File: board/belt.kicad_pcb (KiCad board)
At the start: 2 copper layers, 21 parts, among them J1 USB_B_Micro, J2 USB_B_Micro, J3 USB_B_Micro, J4 USB_B_Micro, Q1 BSS138, Q2 BSS138, SW1 SW_SPST, SW2 SW_Push, U1 Teensy4.0, U2 Adafruit_BNO055

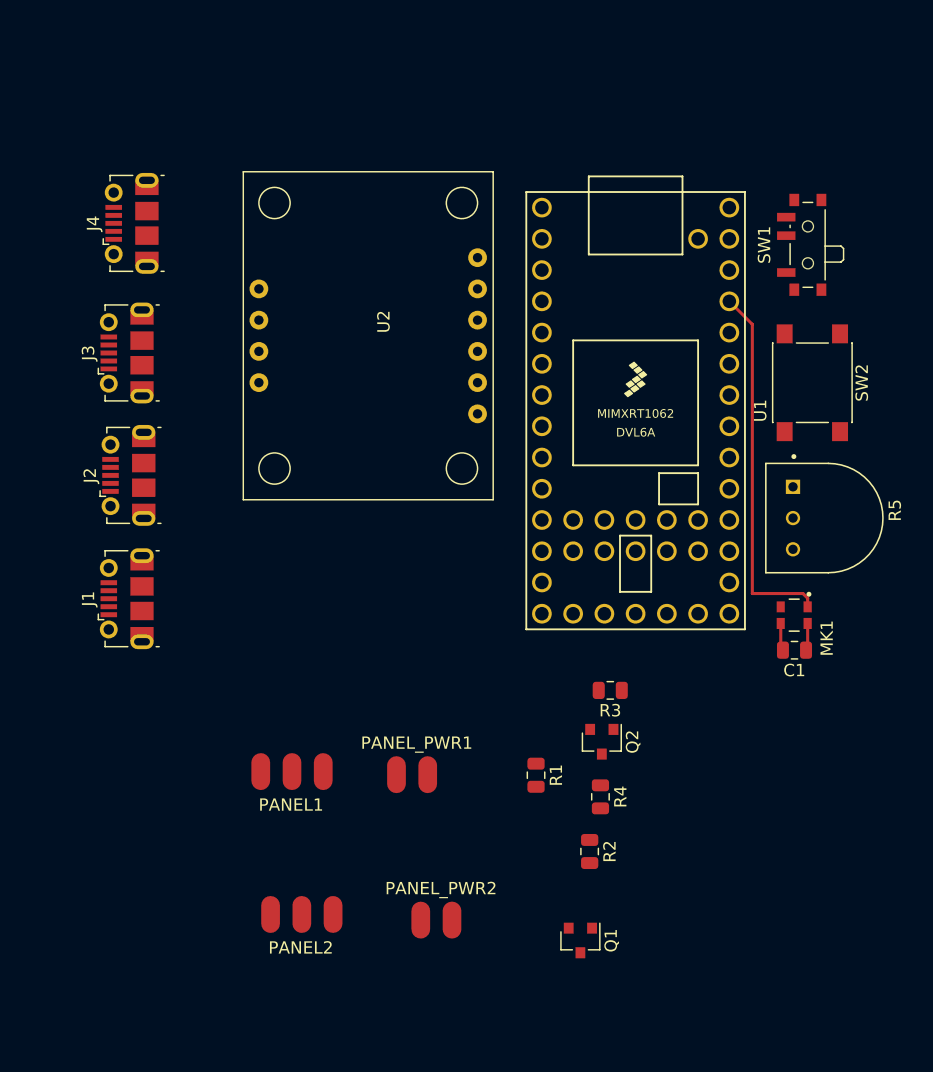
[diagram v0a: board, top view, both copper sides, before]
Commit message: first pass at pcb layout; also start looking into adding an NPN switch so that LED current doesn't have to travel through the rest of the board (concerns about wire thickness, heat, etc.)
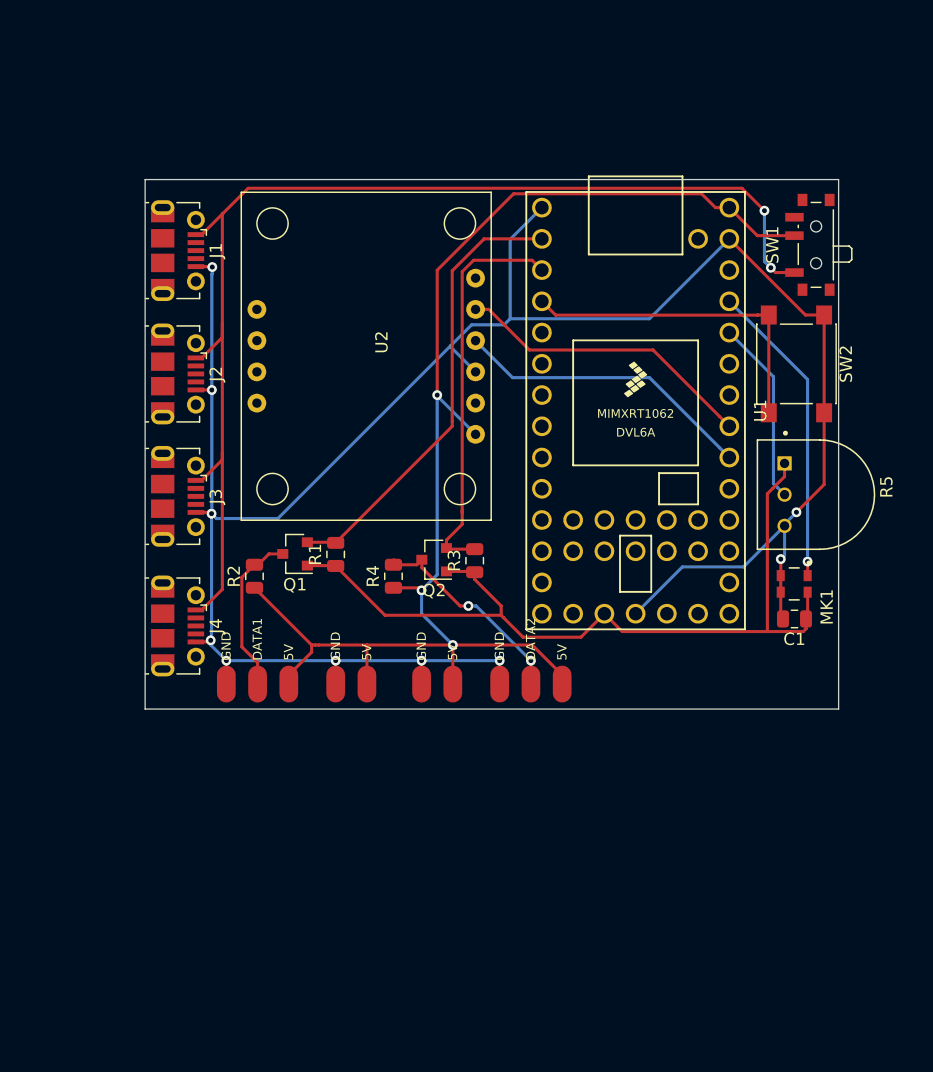
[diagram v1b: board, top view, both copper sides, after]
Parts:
- removed PANEL2: Conn_01x03, Pad_SMD:Pad_SMD_01x03
- added DATA2: Conn_01x03, Pad_SMD:Pad_SMD_01x03, F.Cu at (151.1, 113.0)
- moved Q1 39.1 mm to (132.0, 102.4), turned to 180 degrees
- moved R2 35.3 mm to (128.7, 104.3), turned to 90 degrees
- moved J4 33.0 mm to (122.4, 108.3), turned to 270 degrees
- moved J1 28.6 mm to (122.4, 77.8), turned to 270 degrees
- moved R4 24.6 mm to (140.0, 104.3), turned to 90 degrees
- moved R1 24.2 mm to (135.3, 102.5), turned to 90 degrees
- moved Q2 20.1 mm to (143.3, 102.9), turned to 180 degrees
- moved PANEL_PWR2 16.5 mm to (143.5, 113.0)
- moved R3 15.3 mm to (146.6, 103.0), turned to 90 degrees
- moved J3 12.4 mm to (122.4, 97.8), turned to 270 degrees
- moved J2 9.18 mm to (122.4, 87.8), turned to 270 degrees
- moved DATA1 7.65 mm to (128.9, 113.0)
- moved PANEL_PWR1 7.14 mm to (136.5, 113.0)
- moved C1 2.54 mm to (172.6, 107.7)
- moved MK1 2.54 mm to (172.5, 104.9)
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- renumbered PANEL1 to DATA1
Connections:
- J1 pad 2: (no net) -> Net-(J1-Pad2)
- J1 pad 3: (no net) -> Net-(J1-Pad3)
- J1 pad 4: (no net) -> Net-(J1-Pad4)
- J2 pad 2: (no net) -> Net-(J2-Pad2)
- J2 pad 3: (no net) -> Net-(J2-Pad3)
- J2 pad 4: (no net) -> Net-(J2-Pad4)
- J3 pad 2: (no net) -> Net-(J3-Pad2)
- J3 pad 3: (no net) -> Net-(J3-Pad3)
- J3 pad 4: (no net) -> Net-(J3-Pad4)
- J4 pad 2: (no net) -> Net-(J4-Pad2)
- J4 pad 3: (no net) -> Net-(J4-Pad3)
- J4 pad 4: (no net) -> Net-(J4-Pad4)
- R5 pad 1: VDD -> +3V3
- U1 pad 10: (no net) -> Net-(U1-Pad10)
- U1 pad 11: (no net) -> Net-(U1-Pad11)
- U1 pad 12: (no net) -> Net-(U1-Pad12)
- U1 pad 13: (no net) -> Net-(U1-Pad13)
- U1 pad 14: (no net) -> Net-(U1-Pad14)
- U1 pad 15: (no net) -> Net-(U1-Pad15)
- U1 pad 18: (no net) -> Net-(U1-Pad18)
- U1 pad 19: (no net) -> Net-(U1-Pad19)
- U1 pad 20: (no net) -> Net-(U1-Pad20)
- U1 pad 21: (no net) -> Net-(U1-Pad21)
- U1 pad 22: (no net) -> Net-(U1-Pad22)
- U1 pad 23: (no net) -> Net-(U1-Pad23)
- U1 pad 24: (no net) -> Net-(U1-Pad24)
- U1 pad 25: (no net) -> /MOTION_SDA
- U1 pad 26: (no net) -> /MOTION_SCL
- U1 pad 27: (no net) -> Net-(U1-Pad27)
- U1 pad 28: (no net) -> Net-(U1-Pad28)
- U1 pad 31: (no net) -> Net-(U1-Pad31)
- U1 pad 34: (no net) -> Net-(U1-Pad34)
- U1 pad 35: (no net) -> Net-(U1-Pad35)
- U1 pad 36: (no net) -> Net-(U1-Pad36)
- U1 pad 37: (no net) -> Net-(U1-Pad37)
- U1 pad 38: (no net) -> Net-(U1-Pad38)
- U1 pad 39: (no net) -> Net-(U1-Pad39)
- U1 pad 40: (no net) -> Net-(U1-Pad40)
- U1 pad 41: (no net) -> Net-(U1-Pad41)
- U1 pad 42: (no net) -> Net-(U1-Pad42)
- U1 pad 43: (no net) -> Net-(U1-Pad43)
- U1 pad 44: (no net) -> Net-(U1-Pad44)
- U1 pad 5: (no net) -> Net-(U1-Pad5)
- U1 pad 6: (no net) -> Net-(U1-Pad6)
- U1 pad 7: (no net) -> Net-(U1-Pad7)
- U1 pad 8: (no net) -> Net-(U1-Pad8)
- U1 pad 9: (no net) -> Net-(U1-Pad9)
- U2 pad 1: (no net) -> VDD
- U2 pad 10: (no net) -> Net-(U2-Pad10)
- U2 pad 2: (no net) -> Net-(U2-Pad2)
- U2 pad 3: (no net) -> GND
- U2 pad 4: (no net) -> /MOTION_SDA
- U2 pad 5: (no net) -> /MOTION_SCL
- U2 pad 6: (no net) -> Net-(U2-Pad6)
- U2 pad 7: (no net) -> Net-(U2-Pad7)
- U2 pad 8: (no net) -> Net-(U2-Pad8)
- U2 pad 9: (no net) -> Net-(U2-Pad9)
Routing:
- net GND: track 2.25 -> 185.0 mm, vias 0 -> 10
- net VDD: track 0.00 -> 111.4 mm, vias 0 -> 3
- net VBUS: track 0.00 -> 97.9 mm, vias 0 -> 2
- net +3V3: track 2.23 -> 68.6 mm
- net /DATA1: track 0.00 -> 36.9 mm
- net /DATA2: track 0.00 -> 32.8 mm
- net /BUTTON: track 0.00 -> 26.9 mm
- net /MOTION_SDA: track 0.00 -> 24.6 mm
- net /MOTION_SCL: track 0.00 -> 24.6 mm
- net Net-(PANEL2-Pad2): track 0.00 -> 17.4 mm, vias 0 -> 2
- net /THUMBDIAL: track 0.00 -> 15.0 mm
- net Net-(PANEL1-Pad2): track 0.00 -> 13.0 mm
- net /MICROPHONE: track 29.9 -> 24.9 mm, vias 0 -> 1
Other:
- board outline added: 56.4 x 43.1 mm
- board text added: "5V"
- board text added: "GND"

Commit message: alternate layout with thick wires and switch on top to avoid needing a transistor to switch power nearby (would likely need a large transistor with a heatsink to manage the current)
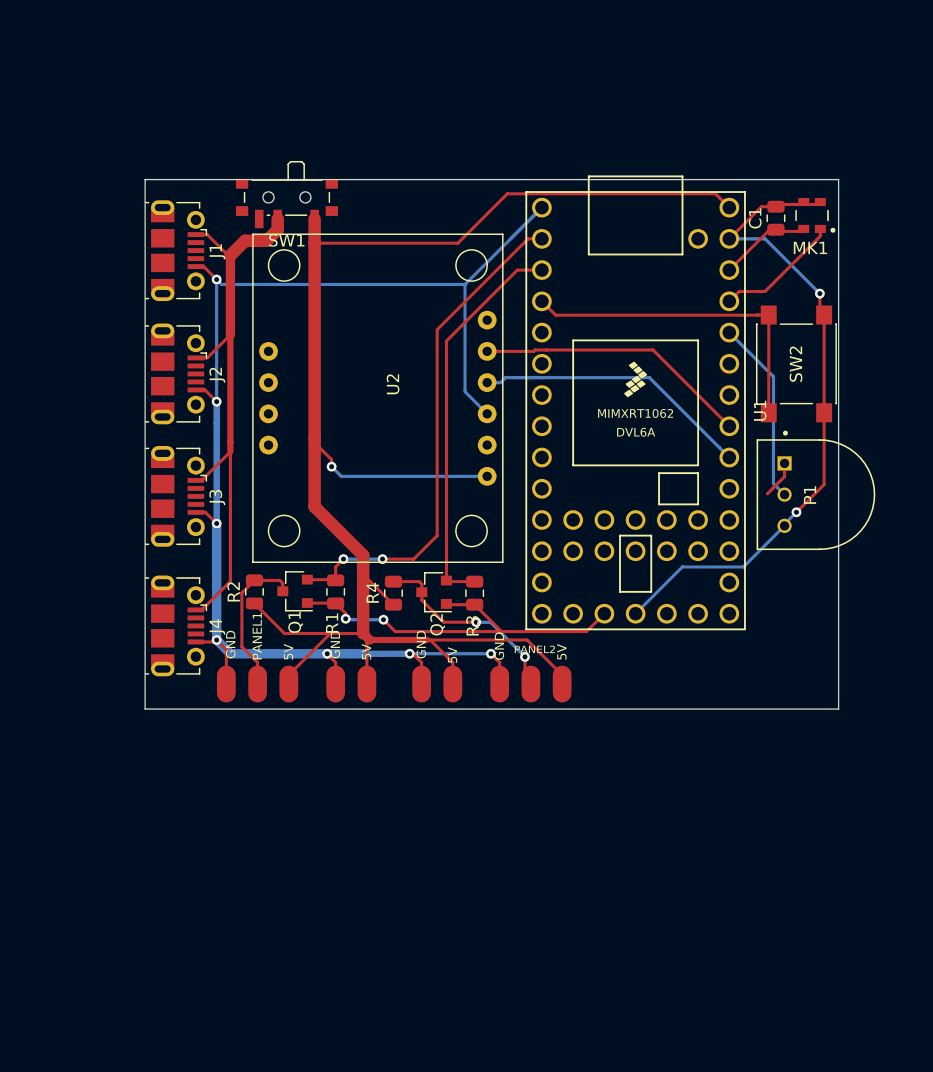
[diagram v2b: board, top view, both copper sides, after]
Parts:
- moved SW1 42.8 mm to (131.3, 73.8), turned to 180 degrees
- moved C1 32.6 mm to (171.1, 75.2), turned to 90 degrees
- moved MK1 30.0 mm to (174.0, 74.9), turned to 180 degrees
- moved U2 3.54 mm to (150.1, 86.1)
- moved R1 3.05 mm to (135.3, 105.5)
- moved Q1 3.04 mm to (132.0, 105.5)
- moved Q2 2.64 mm to (143.3, 105.6)
- moved R3 2.64 mm to (146.6, 105.6)
- moved R4 1.37 mm to (140.0, 105.6)
- moved R2 1.27 mm to (128.7, 105.5)
- renumbered R5 to P1, DATA1 to PANEL1, DATA2 to PANEL2
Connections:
- C1 pad 1: +3V3 -> /MIC_PWR
- MK1 pad 4: +3V3 -> /MIC_PWR
- SW1 pad 1: VBUS -> VDD
- SW1 pad 2: VDD -> VBUS
- U1 pad 31: Net-(U1-Pad31) -> /MIC_PWR
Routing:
- net VBUS: track 97.9 -> 49.1 mm, vias 2 -> 0
- net +3V3: track 68.6 -> 34.6 mm, vias 0 -> 2
- net VDD: track 111.4 -> 133.7 mm, vias 3 -> 1
- net GND: track 185.0 -> 170.0 mm, vias 10 -> 9
- net /MICROPHONE: track 24.9 -> 10.2 mm, vias 1 -> 0
- net /MIC_PWR: track 0.00 -> 7.38 mm
- net /DATA1: track 36.9 -> 41.2 mm, vias 0 -> 2
- net /MOTION_SCL: track 24.6 -> 22.3 mm
- net Net-(PANEL2-Pad2): track 17.4 -> 16.4 mm
- net /DATA2: track 32.8 -> 32.1 mm
- net Net-(PANEL1-Pad2): track 13.0 -> 12.4 mm
- net /MOTION_SDA: track 24.6 -> 25.1 mm

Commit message: shuffle things around some more
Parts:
- added REF**: MountingHole_2.1mm, MountingHole:MountingHole_2.1mm, F.Cu at (178.4, 71.1)
- added REF**: MountingHole_2.1mm, MountingHole:MountingHole_2.1mm, F.Cu at (118.7, 69.8)
- added REF**: MountingHole_2.1mm, MountingHole:MountingHole_2.1mm, F.Cu at (120.0, 116.2)
- added REF**: MountingHole_2.1mm, MountingHole:MountingHole_2.1mm, F.Cu at (173.4, 112.4)
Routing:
- net +3V3: track 34.6 -> 57.7 mm
- net GND: track 170.0 -> 184.8 mm
- net Net-(PANEL2-Pad2): track 16.4 -> 17.6 mm

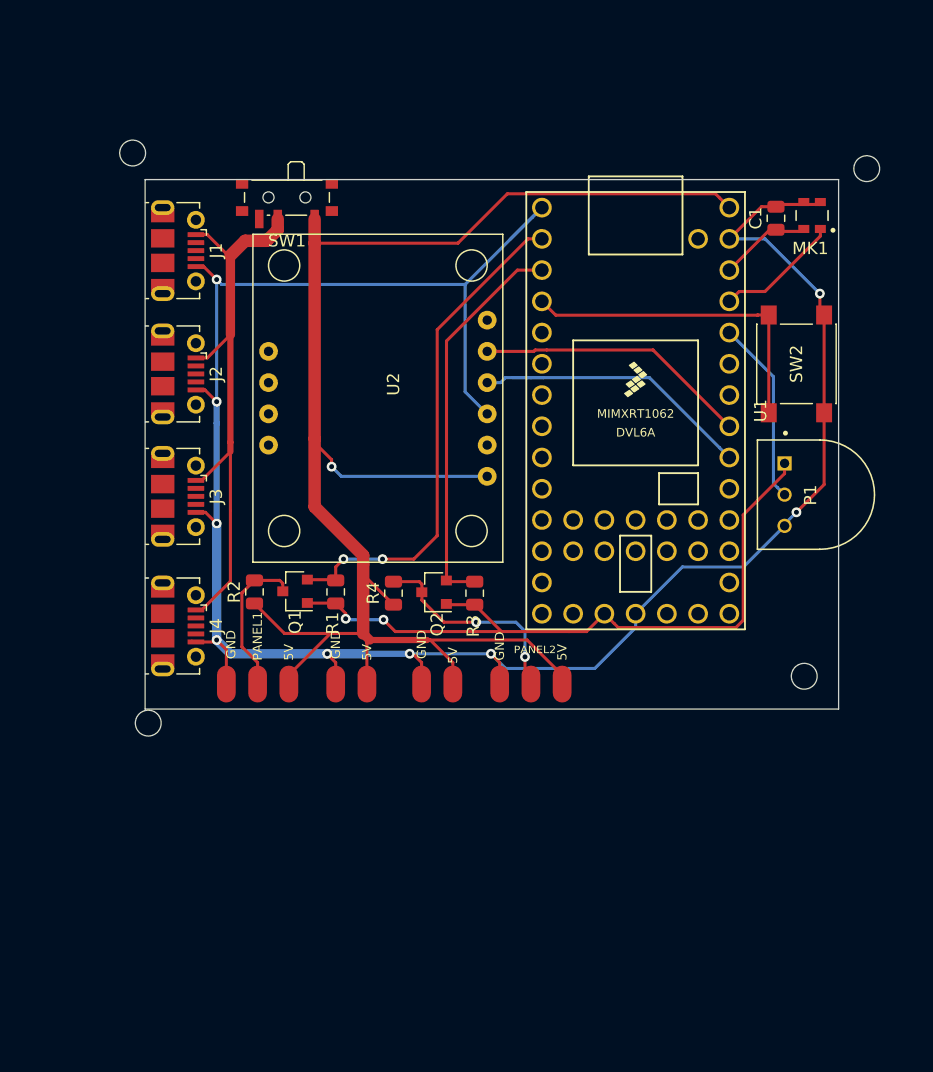
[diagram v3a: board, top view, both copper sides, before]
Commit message: polish board edges; add mounting points
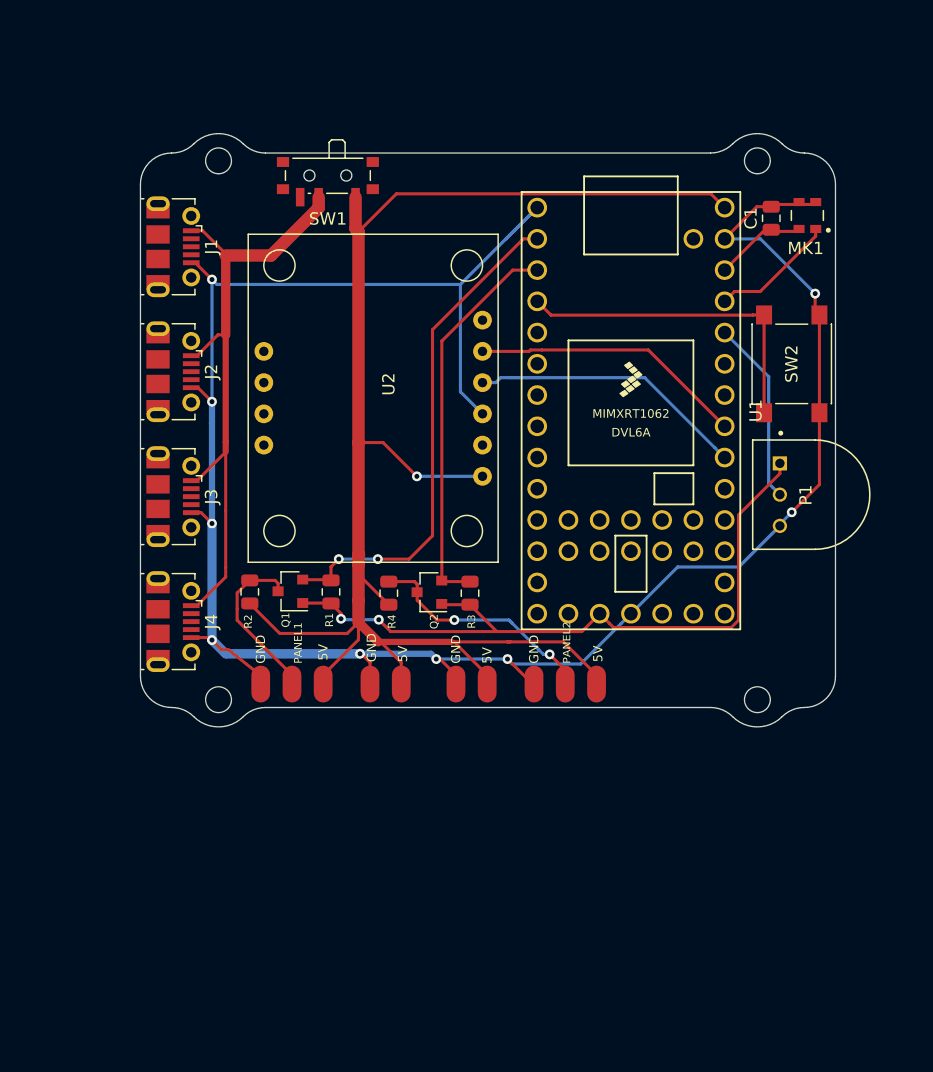
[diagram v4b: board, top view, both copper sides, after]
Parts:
- removed the REF** at (178.4, 71.1)
- removed the REF** at (118.7, 69.8)
- removed the REF** at (120.0, 116.2)
- added REF**: MountingHole_2.1mm, MountingHole:MountingHole_2.1mm, F.Cu at (169.5, 70.5)
- added REF**: MountingHole_2.1mm, MountingHole:MountingHole_2.1mm, F.Cu at (125.7, 70.5)
- added REF**: MountingHole_2.1mm, MountingHole:MountingHole_2.1mm, F.Cu at (125.7, 114.3)
- moved REF** 4.26 mm to (169.5, 114.3)
- moved SW1 3.77 mm to (134.6, 72.0)
- moved PANEL1 2.79 mm to (131.7, 113.0)
- moved PANEL2 2.79 mm to (153.9, 113.0)
- moved PANEL_PWR2 2.79 mm to (146.3, 113.0)
- moved PANEL_PWR1 2.79 mm to (139.3, 113.0)
- moved J4 0.52 mm to (122.0, 108.0)
- moved J1 0.49 mm to (122.0, 77.5)
- moved J2 0.42 mm to (122.0, 87.6)
- moved J3 0.38 mm to (122.0, 97.8)
- moved C1 0.38 mm to (170.7, 75.2)
- moved MK1 0.38 mm to (173.6, 74.9)
- moved P1 0.38 mm to (174.2, 97.6)
- moved Q1 0.38 mm to (131.6, 105.5)
- moved Q2 0.38 mm to (142.9, 105.6)
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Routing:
- net VDD: track 133.7 -> 129.2 mm
- net VBUS: track 49.1 -> 51.6 mm
- net Net-(PANEL2-Pad2): track 17.6 -> 19.3 mm
- net Net-(PANEL1-Pad2): track 12.4 -> 13.8 mm
- net GND: track 184.8 -> 186.0 mm
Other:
- board size 56.4 x 43.1 mm -> 56.5 x 48.2 mm

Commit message: move pot and button ports to be nearer by on teensy
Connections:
- U1 pad 22: Net-(U1-Pad22) -> /THUMBDIAL
- U1 pad 29: /THUMBDIAL -> /BUTTON
- U1 pad 4: /BUTTON -> Net-(U1-Pad4)
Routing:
- net /BUTTON: track 26.9 -> 12.7 mm
- net /THUMBDIAL: track 15.0 -> 6.46 mm
